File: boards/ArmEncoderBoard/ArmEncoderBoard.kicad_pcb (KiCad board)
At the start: 2 copper layers, 34 x 34 mm, 34 parts, among them J1 Conn_01x05, Q1 SS8050, Q2 SS8050, U1 SN74LVC2G17DBVR, U2 AS5045B

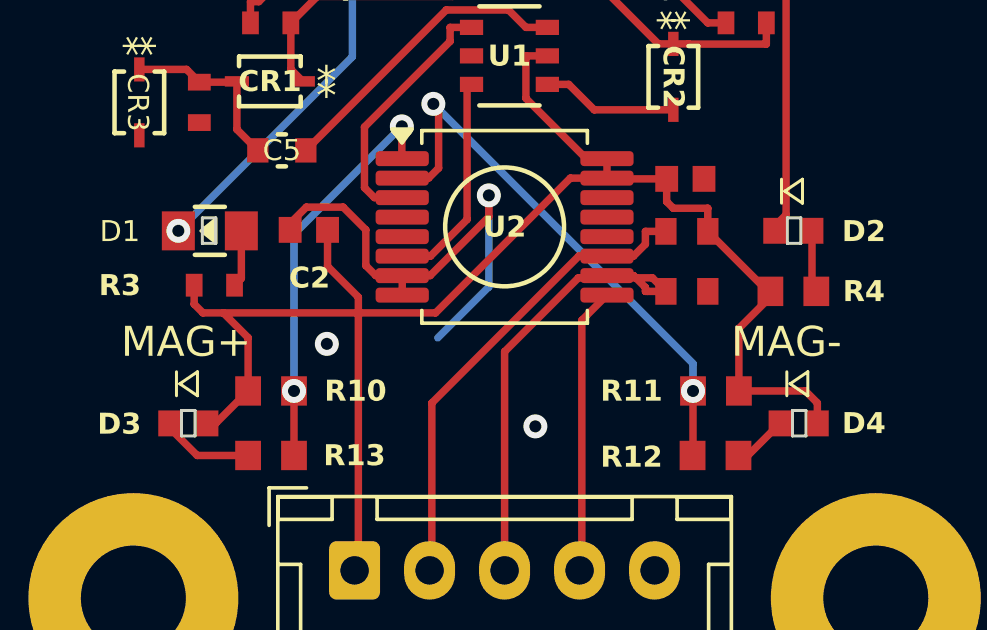
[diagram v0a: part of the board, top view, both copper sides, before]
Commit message: Debug and re-design leg encoder and leg robot board
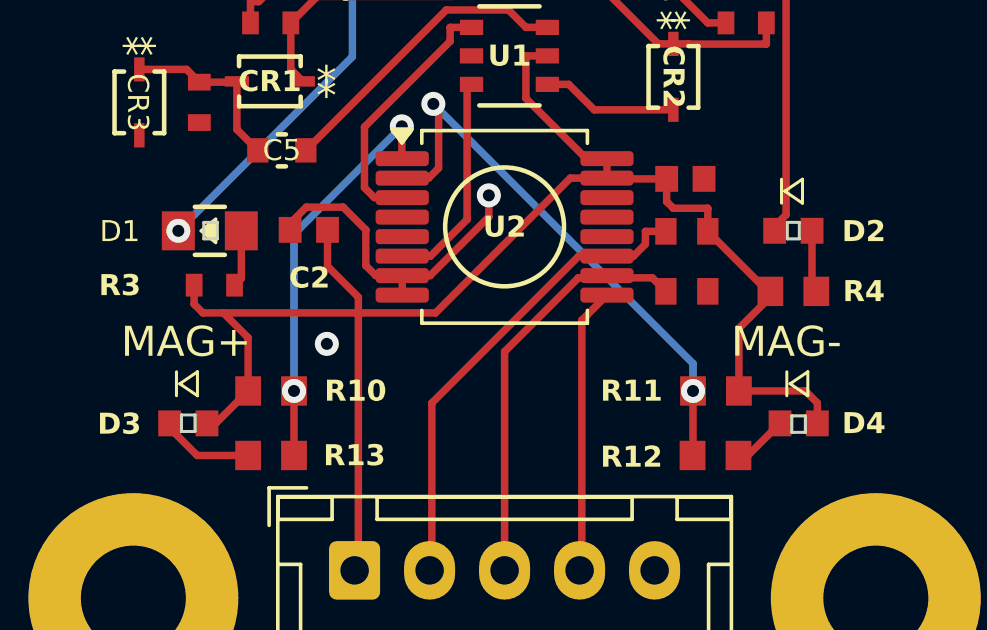
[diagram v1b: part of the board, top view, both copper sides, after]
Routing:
- net GND: track 19.8 -> 14.4 mm
- net SCK: track 16.1 -> 13.9 mm
- net (no net): vias 1 -> 0
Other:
- outline, holes or cut-outs redrawn
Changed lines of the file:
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@@
 	)
 	(gr_rect
-		(start 148.15 81.75)
-		(end 148.6 82.6)
+		(start 128.7 81.9)
+		(end 129.15 82.45)
 		(stroke
 			(width 0.1)
@@
 	)
 	(gr_rect
-		(start 127.9551 88.1698)
-		(end 128.4051 89.0198)
+		(start 127.9551 88.3198)
+		(end 128.4051 88.8698)
 		(stroke
 			(width 0.1)
@@
 	)
 	(gr_rect
-		(start 148.3204 88.1698)
-		(end 148.7704 89.0198)
-		(stroke
-			(width 0.1)
-			(type default)
-		)
-		(fill no)
-		(layer "Edge.Cuts")
-	)
-	(gr_rect
-		(start 128.65 81.75)
-		(end 129.1 82.6)
+		(start 148.15 81.9)
+		(end 148.55 82.45)
 		(stroke
 			(width 0.1)
@@
 		(layer "Edge.Cuts")
 	)
+	(gr_rect
+		(start 148.3 88.35)
+		(end 148.75 88.9)
+		(stroke
+			(width 0.1)
+			(type default)
+		)
+		(fill no)
+		(layer "Edge.Cuts")
+	)
 	(gr_text "MAG+"
 		(at 125.938753 86.4698 0)
@@
 		)
 	)
-	(via
-		(at 139.75 88.7)
-		(size 0.8)
-		(drill 0.4)
-		(layers "F.Cu" "B.Cu")
-		(net 0)
-	)
 	(segment
 		(start 141.184726 83.749)
@@
 	)
 	(segment
-		(start 143.0256 83.675)
-		(end 143.4192 84.0686)
-		(width 0.25)
-		(layer "F.Cu")
-		(net 2)
-	)
-	(segment
 		(start 138.725 86.208726)
 		(end 138.725 93.5)
@@
 	)
 	(segment
-		(start 142.1375 83.675)
-		(end 143.0256 83.675)
-		(width 0.25)
-		(layer "F.Cu")
-		(net 2)
-	)
-	(segment
-		(start 143.4911 84.2)
-		(end 143.4192 84.2)
-		(width 0.25)
-		(layer "F.Cu")
-		(net 2)
-	)
-	(segment
-		(start 144.1015 84.2)
-		(end 143.4911 84.2)
-		(width 0.25)
-		(layer "F.Cu")
-		(net 2)
-	)
-	(segment
 		(start 143.6505 83.749)
 		(end 141.184726 83.749)
-		(width 0.25)
-		(layer "F.Cu")
-		(net 2)
-	)
-	(segment
-		(start 143.4192 84.0686)
-		(end 143.4192 84.2)
 		(width 0.25)
 		(layer "F.Cu")
@@
 		(width 0.25)
 		(layer "B.Cu")
-		(net 8)
-	)
-	(segment
-		(start 138.2 81)
-		(end 138.2 84.05)
-		(width 0.25)
-		(layer "B.Cu")
-		(net 8)
-	)
-	(segment
-		(start 138.2 84.05)
-		(end 136.5 85.75)
-		(width 0.25)
-		(layer "B.Cu")
